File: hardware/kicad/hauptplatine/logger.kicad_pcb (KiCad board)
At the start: 4 copper layers, 121 x 121 mm, 165 parts, among them J201 Solar 1, J202 Solar 2, J301 USB-C, J302 Debug (SWD + Serial1), J501 Wägezelle, J601 Mikrofon, J701 DS18B20 Nr. 1, J702 DS18B20 Nr. 2, J703 BME280, J704 Erweiterung, J801 Strommessung, Q501 S8550, Q801 FS8205, Q802 AO3400A, Q803 AO3400A, SW301 Reset, SW302 BOOT, SW303 Service, SW304 MRS03-B-3, U201 BQ25185DLHR, U202 RT9080-33GJ5, U203 TPS22917DBV, U204 TPS70933DBV, U301 STM32F411CEU6, U302 USBLC6-2SC6, U401 Ra-01SH, U402 64 Mbit SOIC-8 208 mil, U501 TPS61240DRVR, U502 HX711, U601 TLV9001IDBVR, U801 HY2111-GB, U802 TMP390A2DRL, U803 TMP390A2DRL, Y301 25MHz 12pF, Y302 32,768k 7pF

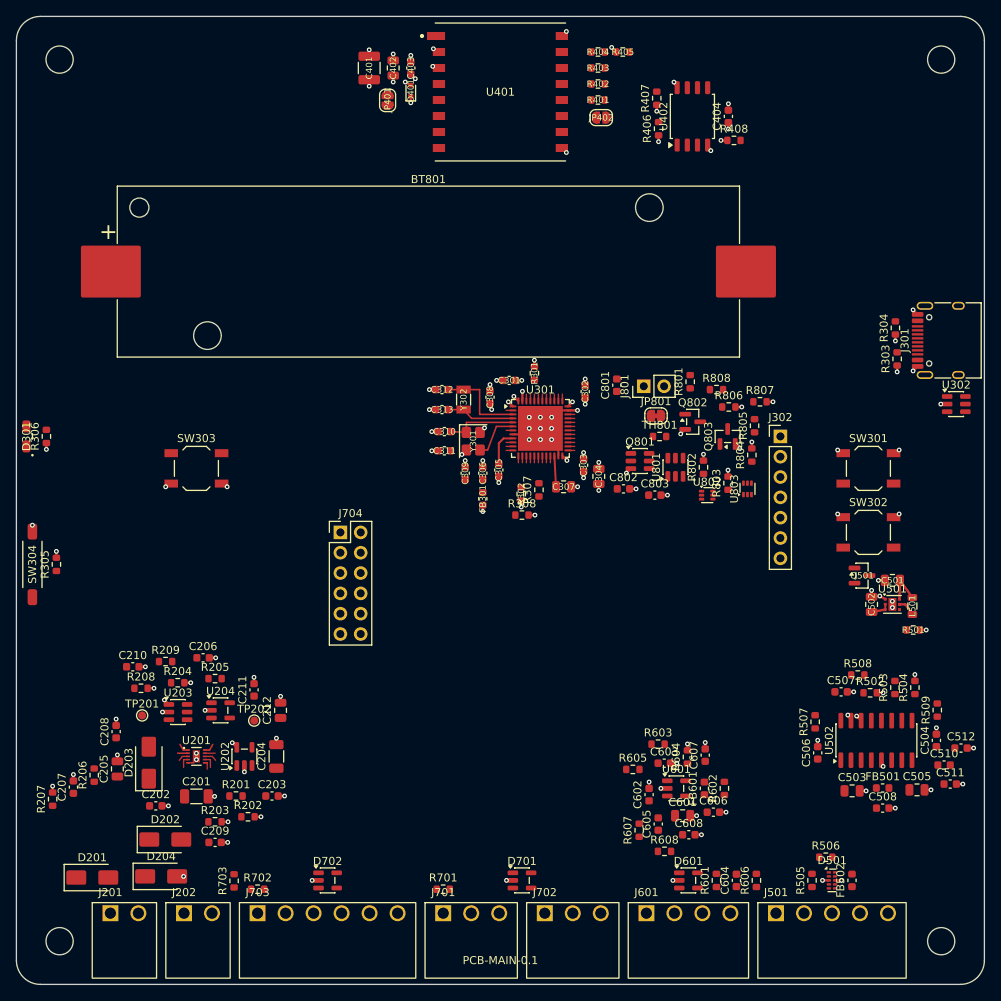
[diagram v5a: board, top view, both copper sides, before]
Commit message: HW-07: zwei Mikrofone am Audio-ADC TLV320ADC3101, I2S3, RJ45 J5; HW-08: Platine nur Rahmen, Layout extern; Pflichtenheft und Übergabepaket für den Layouter; ERC 0, Netzprüfung 187/187, Pin/Footprint 0
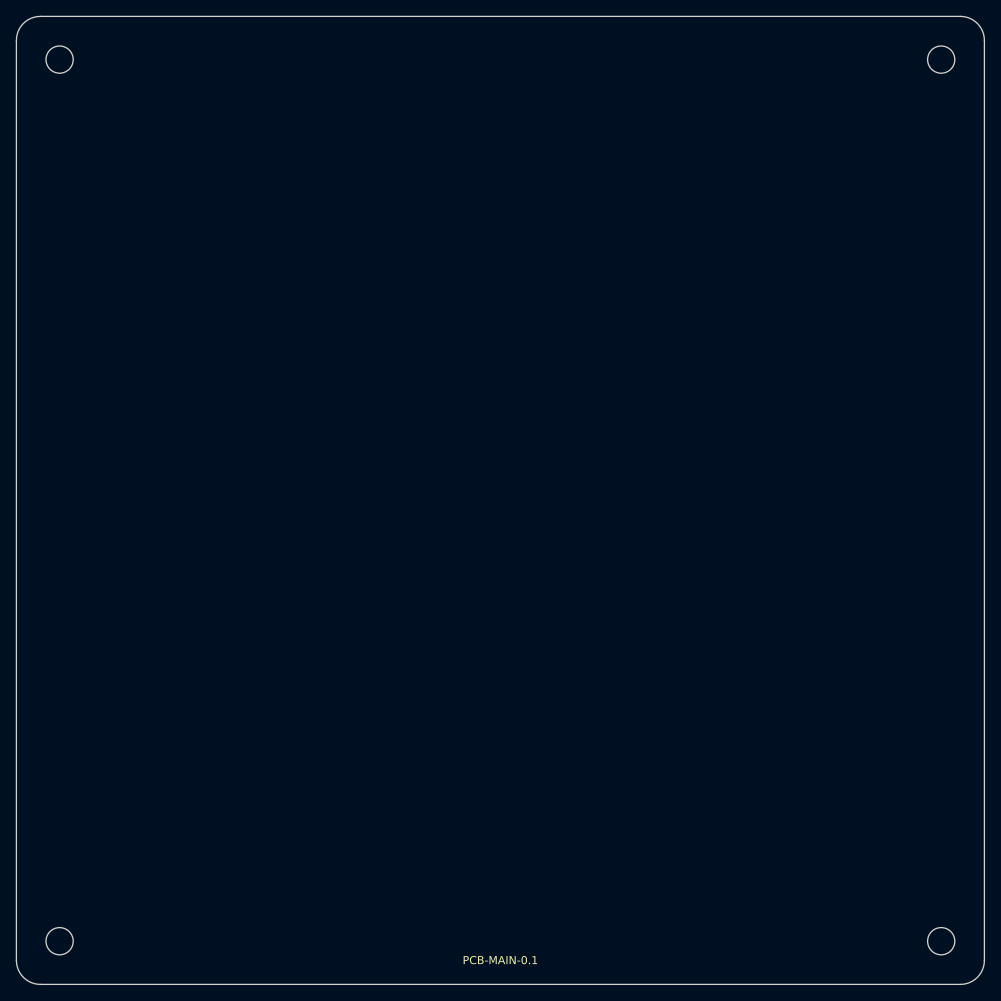
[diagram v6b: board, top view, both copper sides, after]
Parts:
- removed BT801: 18650 3,6 V, Battery:BatteryHolder_Keystone_1042_1x18650
- removed C201: 4,7µ 50V X7R, Capacitor_SMD:C_1206_3216Metric
- removed C202: 100n 50V, Capacitor_SMD:C_0603_1608Metric
- removed C203, C207, C301, C302, C303, C305, C308, C309, C403, C404, C504, C506, C507, C508, C510, C602, C607, C801, C802, C803: 100n, Capacitor_SMD:C_0603_1608Metric
- removed C204: 22µ 25V X5R, Capacitor_SMD:C_1206_3216Metric
- removed C205: 4,7µ, Capacitor_SMD:C_0805_2012Metric
- removed C206: 10n, Capacitor_SMD:C_0603_1608Metric
- removed C208, C209: 2,2µ 16V X7R, Capacitor_SMD:C_0603_1608Metric
- removed C210: 1n, Capacitor_SMD:C_0603_1608Metric
- removed C211, C306, C603: 1µ, Capacitor_SMD:C_0603_1608Metric
- removed C212: 4,7µ 16V X7R, Capacitor_SMD:C_0805_2012Metric
- removed C304, C402, C502, C503, C505: 10µ 10V X5R, Capacitor_SMD:C_0805_2012Metric
- removed C307: 4,7µ X7R, Capacitor_SMD:C_0805_2012Metric
- removed C310, C311: 18p C0G, Capacitor_SMD:C_0603_1608Metric
- removed C312, C313: 8,2p C0G, Capacitor_SMD:C_0603_1608Metric
- removed C401: 100µ 6,3V X5R, Capacitor_SMD:C_1210_3225Metric
- removed C501: 4,7µ 16V X5R, Capacitor_SMD:C_0805_2012Metric
- removed C511, C512, C606, C608: 10n C0G, Capacitor_SMD:C_0603_1608Metric
- removed C601: 22µ 10V X5R, Capacitor_SMD:C_0805_2012Metric
- removed C604: 220n X7R, Capacitor_SMD:C_0603_1608Metric
- removed C605: 22n C0G, Capacitor_SMD:C_0603_1608Metric
- removed D201, D202, D203: SS34, Diode_SMD:D_SMA
- removed D204: SMAJ12A, Diode_SMD:D_SMA
- removed D301: LTST-S220KGKT, Bienen:LED_Lite-On_LTST-S220_SideView
- removed D401: TVS 3,3V, Diode_SMD:D_SOD-523
- removed D501: TPD4E05U06DQAR, Package_SON:USON-10_2.5x1.0mm_P0.5mm
- removed D601, D701, D702: ESDS304DBVR, Package_TO_SOT_SMD:SOT-23-5
- removed FB301, FB501, FB601: 600R@100MHz, Inductor_SMD:L_0603_1608Metric
- removed FB502: Ferrit ≤ 0,1 Ω, Inductor_SMD:L_0603_1608Metric
- removed J201: Solar 1, Bienen:DEGSON_15EDGRC-3.5-02P
- removed J202: Solar 2, Bienen:DEGSON_15EDGRC-3.5-02P
- removed J301: USB-C, Connector_USB:USB_C_Receptacle_HRO_TYPE-C-31-M-12
- removed J302: Debug (SWD + Serial1), Connector_PinHeader_2.54mm:PinHeader_1x07_P2.54mm_Vertical
- removed J501: Wägezelle, Bienen:DEGSON_15EDGRC-3.5-05P
- removed J601: Mikrofon, Bienen:DEGSON_15EDGRC-3.5-04P
- removed J701: DS18B20 Nr. 1, Bienen:DEGSON_15EDGRC-3.5-03P
- removed J702: DS18B20 Nr. 2, Bienen:DEGSON_15EDGRC-3.5-03P
- removed J703: BME280, Bienen:DEGSON_15EDGRC-3.5-06P
- removed J704: Erweiterung, Connector_PinHeader_2.54mm:PinHeader_2x06_P2.54mm_Vertical
- removed J801: Strommessung, Connector_PinHeader_2.54mm:PinHeader_1x02_P2.54mm_Vertical
- removed JP401: TXEN, Jumper:SolderJumper-2_P1.3mm_Open_RoundedPad1.0x1.5mm
- removed JP402: RXEN, Jumper:SolderJumper-2_P1.3mm_Open_RoundedPad1.0x1.5mm
- removed JP801: Messbrücke B+, Jumper:SolderJumper-2_P1.3mm_Bridged_RoundedPad1.0x1.5mm
- removed L501: 1µ, Inductor_SMD:L_0805_2012Metric
- removed Q501: S8550, Package_TO_SOT_SMD:SOT-23
- removed Q801: FS8205, Package_TO_SOT_SMD:SOT-23-6
- removed Q802, Q803: AO3400A, Package_TO_SOT_SMD:SOT-23
- removed R201: 3,3M, Resistor_SMD:R_0603_1608Metric
- removed R202: 470k, Resistor_SMD:R_0603_1608Metric
- removed R203: 2,0k 1%, Resistor_SMD:R_0603_1608Metric
- removed R204: 130k 1%, Resistor_SMD:R_0603_1608Metric
- removed R205, R208, R305, R405, R406, R501, R502, R805, R808: 100k, Resistor_SMD:R_0603_1608Metric
- removed R206, R207: 2,2M, Resistor_SMD:R_0603_1608Metric
- removed R209, R507: 0, Resistor_SMD:R_0603_1608Metric
- removed R301, R302, R407, R408: 10k, Resistor_SMD:R_0603_1608Metric
- removed R303, R304: 5,1k, Resistor_SMD:R_0603_1608Metric
- removed R306, R508, R509: 1k, Resistor_SMD:R_0603_1608Metric
- removed R307, R605: 33k, Resistor_SMD:R_0603_1608Metric
- removed R308: 82k, Resistor_SMD:R_0603_1608Metric
- removed R401, R402, R403, R404: 33, Resistor_SMD:R_0603_1608Metric
- removed R503: 20k 1%, Resistor_SMD:R_0603_1608Metric
- removed R504: 8,2k 1%, Resistor_SMD:R_0603_1608Metric
- removed R505, R506, R601, R801: 100, Resistor_SMD:R_0603_1608Metric
- removed R602: 47, Resistor_SMD:R_0603_1608Metric
- removed R603, R604: 47k, Resistor_SMD:R_0603_1608Metric
- removed R606, R607: 9,1k 1%, Resistor_SMD:R_0603_1608Metric
- removed R608: 3,3k, Resistor_SMD:R_0603_1608Metric
- removed R701: 4,7k, Resistor_SMD:R_0603_1608Metric
- removed R702, R703: 1,8k, Resistor_SMD:R_0603_1608Metric
- removed R802: 2k, Resistor_SMD:R_0603_1608Metric
- removed R803, R806: 2,49k 1%, Resistor_SMD:R_0603_1608Metric
- removed R804, R807: 18,7k 1%, Resistor_SMD:R_0603_1608Metric
- removed SW301: Reset, Button_Switch_SMD:SW_SPST_TL3342
- removed SW302: BOOT, Button_Switch_SMD:SW_SPST_TL3342
- removed SW303: Service, Button_Switch_SMD:SW_SPST_TL3342
- removed SW304: MRS03-B-3, Bienen:MiRelay_MRS03_J-Lead_8.5x2.1mm
- removed TH801: 10k B3435, Resistor_SMD:R_0603_1608Metric
- removed TP201: STAT1, TestPoint:TestPoint_Pad_D1.0mm
- removed TP202: STAT2, TestPoint:TestPoint_Pad_D1.0mm
- removed U201: BQ25185DLHR, Bienen:WSON-10-1EP_2.2x2mm_DLH0010A
- removed U202: RT9080-33GJ5, Package_TO_SOT_SMD:TSOT-23-5
- removed U203: TPS22917DBV, Package_TO_SOT_SMD:SOT-23-6
- removed U204: TPS70933DBV, Package_TO_SOT_SMD:SOT-23-5
- removed U301: STM32F411CEU6, Package_DFN_QFN:QFN-48-1EP_7x7mm_P0.5mm_EP5.6x5.6mm
- removed U302: USBLC6-2SC6, Package_TO_SOT_SMD:SOT-23-6
- removed U401: Ra-01SH, Bienen:Ai-Thinker_Ra-01SH
- removed U402: 64 Mbit SOIC-8 208 mil, Package_SO:SOIC-8_5.3x5.3mm_P1.27mm
- removed U501: TPS61240DRVR, Package_SON:WSON-6-1EP_2x2mm_P0.65mm_EP1x1.6mm
- removed U502: HX711, Package_SO:SOIC-16_3.9x9.9mm_P1.27mm
- removed U601: TLV9001IDBVR, Package_TO_SOT_SMD:SOT-23-5
- removed U801: HY2111-GB, Package_TO_SOT_SMD:SOT-23-6
- removed U802, U803: TMP390A2DRL, Package_TO_SOT_SMD:SOT-563
- removed Y301: 25MHz 12pF, Crystal:Crystal_SMD_3225-4Pin_3.2x2.5mm
- removed Y302: 32,768k 7pF, Crystal:Crystal_SMD_3215-2Pin_3.2x1.5mm
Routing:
- net GND: track 81.7 -> 0.00 mm, vias 110 -> 0
- net +3V3: track 24.0 -> 0.00 mm, vias 30 -> 0
- net /MCU/LSE_IN: track 11.2 -> 0.00 mm
- net /MCU/HSE_IN: track 9.04 -> 0.00 mm
- net /MCU/LSE_OUT: track 8.57 -> 0.00 mm
- net SYS: track 6.40 -> 0.00 mm
- net /MCU/HSE_OUT: track 6.16 -> 0.00 mm
- net /MCU/VDDA: track 4.58 -> 0.00 mm
- net /MCU/VCAP: track 3.87 -> 0.00 mm
- net /Waage/5V_WAAGE: track 2.39 -> 0.00 mm
- net /Waage/L_5V: track 2.28 -> 0.00 mm
- net /Versorgung/ILIM: track 1.70 -> 0.00 mm
- net /Versorgung/ISET: track 1.59 -> 0.00 mm
- net CE_LADEN: track 1.55 -> 0.00 mm
- net /Versorgung/VIN_LADER: track 1.41 -> 0.00 mm
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- removed copper zone on In2.Cu, net +3V3
- removed copper zone on In1.Cu, net GND
- removed copper zone on In2.Cu, net GND
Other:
- board text added: "Außenanschlüsse J201/J202, J703, J701/J702, J601 (RJ45), J501 möglichst an einer Kante, ESD direkt dahinter"
- board text added: "Funkkante: Ra-01SH mit IPEX gegenüber den Außenanschlüssen"
- board text added: "Lage der Anschlüsse und Bauteile: Layouter (Lastenheft M5, anschluesse.md 4)"
- board text removed: "Funkkante: Ra-01SH mit IPEX gegenüber den Klemmen"
- board text removed: "J201/J202 Solar - J703 BME280 - J701/J702 DS18B20 - J601 Mikrofon - J501 Waage"
- board text removed: "Klemmenkante (anschluesse.md 4), von links:"
